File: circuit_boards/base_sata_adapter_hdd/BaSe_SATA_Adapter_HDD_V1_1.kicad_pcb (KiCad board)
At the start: 2 copper layers, 61.6 x 15.2 mm, 5 parts, among them J1 821-22-002-10-002101, J2 823-22-014-10-001101, X1 SATA_CONNECTOR_FEM

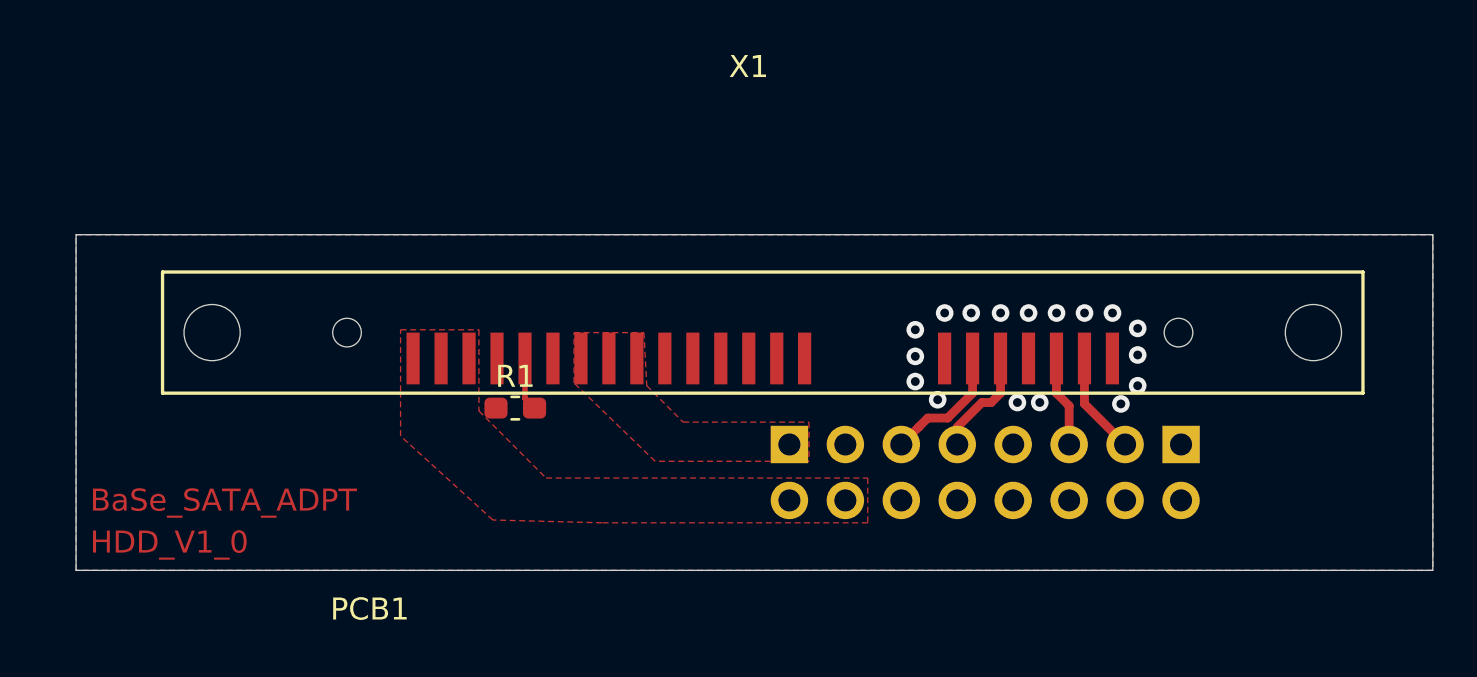
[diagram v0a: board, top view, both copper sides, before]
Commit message: [HW] production ready versions of sata adapter boards
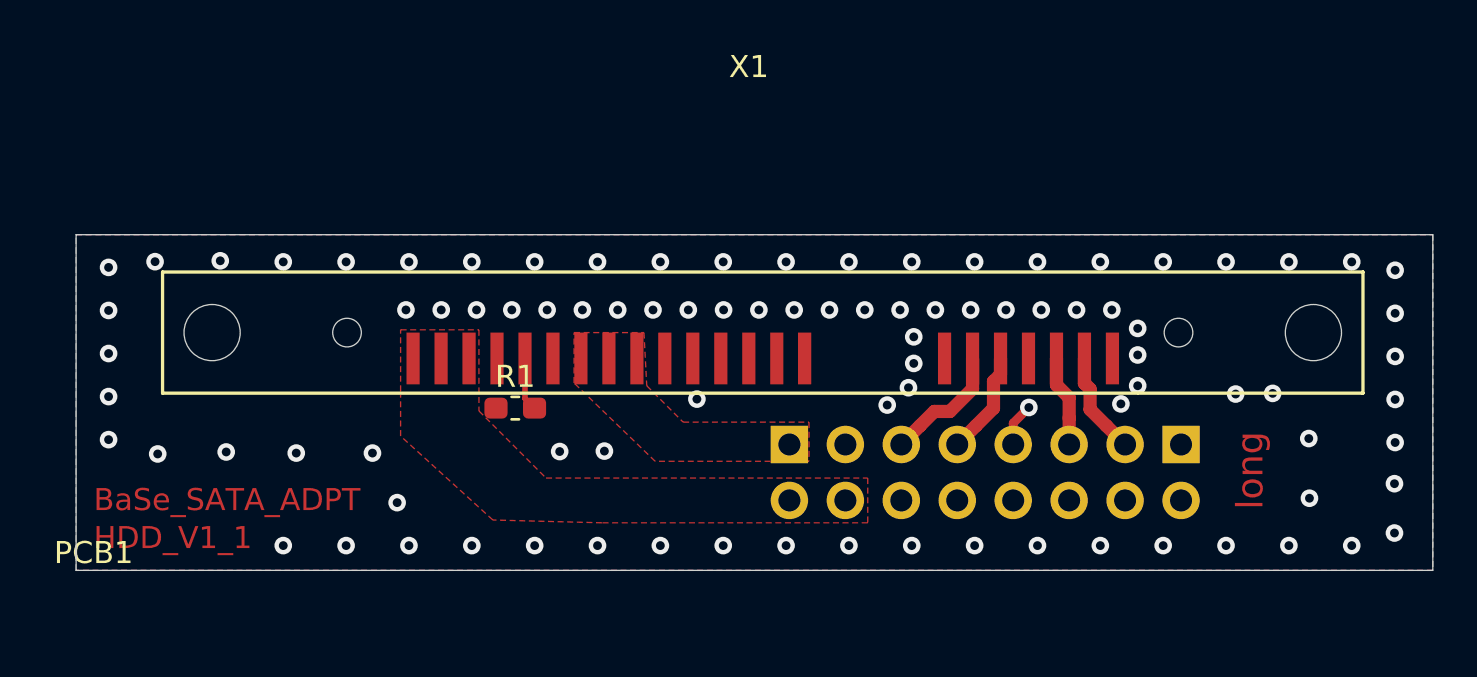
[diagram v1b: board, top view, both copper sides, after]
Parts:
- J1: value 821-22-002-10-002101 -> 821-22-002-10-004101
- PCB1: value BaSe_SATA_Adapter_V1_0 -> BaSe_SATA_Adapter_HDD_V1_1; footprint G7_Labels:BaSe_SATA_Adapter_HDD_V1_0 -> G7_Labels:BaSe_SATA_Adapter_HDD_V1_1
- moved PCB1 12.8 mm to (89.1, 52.7)
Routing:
- net GND: track 0.00 -> 1.97 mm, vias 17 -> 92
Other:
- net class SATA_DIFF: clearance 0.2 -> 0.35; trace_width 0.4 -> 0.6
- board text added: "long"
